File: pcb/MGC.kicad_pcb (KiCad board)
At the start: 2 copper layers, 92.7 x 62.2 mm, 121 parts, among them J1 USB_C_Receptacle, J10 Conn_01x04_Pin, J11 103R012BB100, J12 103R012BB100, J13 103R012BB100, J14 Conn_02x10_Odd_Even, J15 Conn_02x10_Odd_Even, J16 Conn_01x03, J17 Conn_01x01_Pin, J18 Conn_01x02_Pin, J19 Conn_01x02_Pin, J2 Conn_01x02_Pin, J20 Conn_01x02_Pin, J3 103R012BB100, J4 Conn_02x03_Odd_Even, J5 Conn_02x05_Odd_Even, J6 Conn_01x04, J7 103R012BB100, J8 Conn_01x01_Pin, J9 Conn_01x01_Pin, Q10 AO3416, Q11 AO3416, Q12 AO3416, Q13 AO3416, Q9 AO3416, SW0 SW_SPST, SW1 SW_SPST, SW2 SW_SPST, SW3 SW_SPST, SW5 SW_SPST, SW6 SW_DIP_x02, U1 FT230XS, U2 TS3USB30EDGSR, U3 74AHC1G14, U4 TPS2116DRL, U5 LM1117DT-3.3, U6 TBD62783A, U7 MB85RC04V

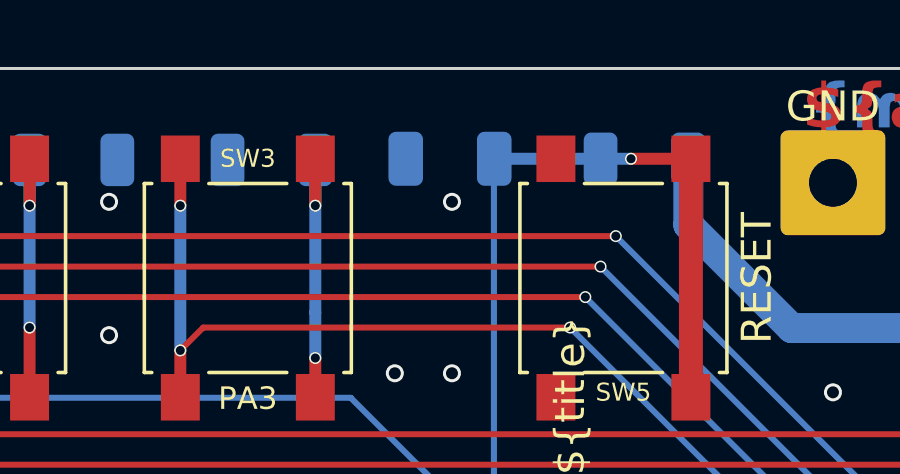
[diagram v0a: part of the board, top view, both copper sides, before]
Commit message: Change reset capacitor device size
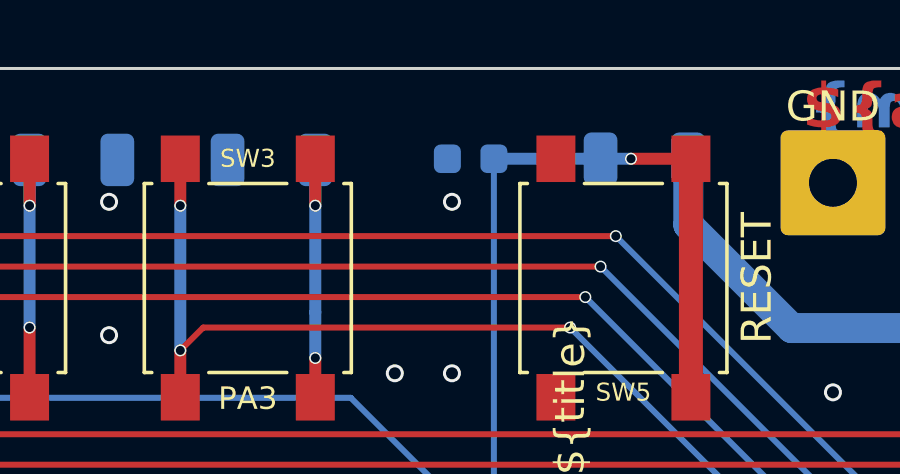
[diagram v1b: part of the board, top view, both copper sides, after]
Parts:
- C2: footprint Capacitor_SMD:C_1206_3216Metric -> Capacitor_SMD:C_0603_1608Metric
- moved C2 0.69 mm to (161.3, 66.5)
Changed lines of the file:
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@@
 		)
 	)
-	(footprint "Capacitor_SMD:C_1206_3216Metric"
+	(footprint "Capacitor_SMD:C_0603_1608Metric"
 		(layer "B.Cu")
-		(at 160.5895 66.51 180)
-		(descr "Capacitor SMD 1206 (3216 Metric), square (rectangular) end terminal, IPC-7351 nominal, (Body size source: IPC-SM-782 page 76, https://www.pcb-3d.com/wordpress/wp-content/uploads/ipc-sm-782a_amendment_1_and_2.pdf), generated with kicad-footprint-generator")
+		(at 161.277 66.51 180)
+		(descr "Capacitor SMD 0603 (1608 Metric), square (rectangular) end terminal, IPC-7351 nominal, (Body size source: IPC-SM-782 page 76, https://www.pcb-3d.com/wordpress/wp-content/uploads/ipc-sm-782a_amendment_1_and_2.pdf), generated with kicad-footprint-generator")
 		(tags "capacitor")
 		(property "Reference" "C2"
-			(at 0 1.506 0)
+			(at 0 1.1304 0)
 			(layer "B.SilkS")
 			(effects
@@
 					(size 0.6 0.6)
 					(thickness 0.12)
+					(bold yes)
 				)
 				(justify mirror)
@@
 		)
 		(property "Value" "10n"
-			(at 0 -1.85 0)
+			(at 0 -1.43 0)
 			(layer "B.Fab")
 			(effects
@@
 		(attr smd)
 		(fp_line
-			(start -0.711252 0.91)
-			(end 0.711252 0.91)
+			(start -0.14058 0.51)
+			(end 0.14058 0.51)
 			(stroke
 				(width 0.12)
@@
 		)
 		(fp_line
-			(start -0.711252 -0.91)
-			(end 0.711252 -0.91)
+			(start -0.14058 -0.51)
+			(end 0.14058 -0.51)
 			(stroke
 				(width 0.12)
@@
 		)
 		(fp_rect
-			(start -2.3 1.15)
-			(end 2.3 -1.15)
+			(start -1.48 0.73)
+			(end 1.48 -0.73)
 			(stroke
 				(width 0.05)
@@
 		)
 		(fp_rect
-			(start -1.6 0.8)
-			(end 1.6 -0.8)
+			(start -0.8 0.4)
+			(end 0.8 -0.4)
 			(stroke
 				(width 0.1)
@@
 			(effects
 				(font
-					(size 0.8 0.8)
-					(thickness 0.12)
+					(size 0.4 0.4)
+					(thickness 0.06)
 				)
 				(justify mirror)
@@
 		)
 		(pad "1" smd roundrect
-			(at -1.475 0 180)
-			(size 1.15 1.8)
+			(at -0.775 0 180)
+			(size 0.9 0.95)
 			(layers "B.Cu" "B.Mask" "B.Paste")
-			(roundrect_rratio 0.217391)
+			(roundrect_rratio 0.25)
 			(net 8 "RESET")
 			(pintype "passive")
 		)
 		(pad "2" smd roundrect
-			(at 1.475 0 180)
-			(size 1.15 1.8)
+			(at 0.775 0 180)
+			(size 0.9 0.95)
 			(layers "B.Cu" "B.Mask" "B.Paste")
-			(roundrect_rratio 0.217391)
+			(roundrect_rratio 0.25)
 			(net 4 "GND")
 			(pintype "passive")
 		)
 		(embedded_fonts no)
-		(model "${KICAD9_3DMODEL_DIR}/Capacitor_SMD.3dshapes/C_1206_3216Metric.step"
+		(model "${KICAD9_3DMODEL_DIR}/Capacitor_SMD.3dshapes/C_0603_1608Metric.step"
 			(offset
 				(xyz 0 0 0)
@@
 	)
 	(segment
-		(start 162.052 90.424)
-		(end 162.052 66.51)
-		(width 0.2)
-		(layer "B.Cu")
-		(net 8)
-	)
-	(segment
 		(start 158.275 91.615)
 		(end 160.861 91.615)
@@
 	)
 	(segment
-		(start 160.861 91.615)
-		(end 162.052 90.424)
+		(start 162.052 90.424)
+		(end 162.052 66.51)
 		(width 0.2)
 		(layer "B.Cu")
@@
 		(layer "B.Cu")
 		(net 8)
+	)
+	(segment
+		(start 160.861 91.615)
+		(end 162.052 90.424)
+		(width 0.2)
+		(layer "B.Cu")
+		(net 8)

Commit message: Device repositioning
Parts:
- moved D15 1.42 mm to (151.4, 82.1), turned to -90 degrees
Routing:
- net VDD: track 349.2 -> 357.5 mm
- net GND: vias 119 -> 118
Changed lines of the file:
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@@
 	(footprint "Diode_SMD:D_MiniMELF"
 		(layer "B.Cu")
-		(at 152.174 80.961)
+		(at 151.384 82.136 -90)
 		(descr "Diode Mini-MELF (SOD-80, LL-34)")
 		(tags "LL34")
 		(property "Reference" "D15"
-			(at 0 2 0)
+			(at 0 2 90)
 			(layer "B.SilkS")
 			(effects
@@
 		)
 		(property "Value" "BAT43"
-			(at 0 -2 0)
+			(at 0 -2 90)
 			(layer "B.Fab")
 			(effects
@@
 		)
 		(property "Datasheet" "~"
-			(at 0 0 180)
+			(at 0 0 90)
 			(unlocked yes)
 			(layer "B.Fab")
@@
 		)
 		(property "Description" "Diode"
-			(at 0 0 180)
+			(at 0 0 90)
 			(unlocked yes)
 			(layer "B.Fab")
@@
 		)
 		(property "Sim.Device" "D"
-			(at 0 0 180)
+			(at 0 0 90)
 			(unlocked yes)
 			(layer "B.Fab")
@@
 		)
 		(property "Sim.Pins" "1=K 2=A"
-			(at 0 0 180)
+			(at 0 0 90)
 			(unlocked yes)
 			(layer "B.Fab")
@@
 		)
 		(property "HTL" "100206"
-			(at 0 0 0)
+			(at 0 0 270)
 			(unlocked yes)
 			(layer "B.Fab")
@@
 		(attr smd)
 		(fp_line
-			(start -2.66 -1.11)
-			(end 1.75 -1.11)
+			(start -2.66 1.11)
+			(end -2.66 -1.11)
 			(stroke
 				(width 0.12)
@@
 		)
 		(fp_line
-			(start -2.66 1.11)
-			(end -2.66 -1.11)
+			(start 1.75 1.11)
+			(end -2.66 1.11)
 			(stroke
 				(width 0.12)
@@
 		)
 		(fp_line
-			(start 1.75 1.11)
-			(end -2.66 1.11)
+			(start -2.66 -1.11)
+			(end 1.75 -1.11)
 			(stroke
 				(width 0.12)
@@
 		)
 		(fp_line
-			(start -2.65 -1.1)
-			(end -2.65 1.1)
+			(start -2.65 1.1)
+			(end 2.65 1.1)
 			(stroke
 				(width 0.05)
@@
 		)
 		(fp_line
-			(start -2.65 1.1)
-			(end 2.65 1.1)
+			(start 2.65 1.1)
+			(end 2.65 -1.1)
 			(stroke
 				(width 0.05)
@@
 		)
 		(fp_line
-			(start 2.65 -1.1)
-			(end -2.65 -1.1)
+			(start -2.65 -1.1)
+			(end -2.65 1.1)
 			(stroke
 				(width 0.05)
@@
 		)
 		(fp_line
-			(start 2.65 1.1)
-			(end 2.65 -1.1)
+			(start 2.65 -1.1)
+			(end -2.65 -1.1)
 			(stroke
 				(width 0.05)
@@
 		)
 		(fp_line
-			(start -1.65 -0.8)
-			(end -1.65 0.8)
+			(start -1.65 0.8)
+			(end 1.65 0.8)
 			(stroke
 				(width 0.1)
@@
 		)
 		(fp_line
-			(start -1.65 0.8)
-			(end 1.65 0.8)
+			(start 1.65 0.8)
+			(end 1.65 -0.8)
 			(stroke
 				(width 0.1)
@@
 		)
 		(fp_line
-			(start -0.75 0)
-			(end -0.35 0)
+			(start 0.25 0.4)
+			(end 0.25 -0.4)
 			(stroke
 				(width 0.1)
@@
 		)
 		(fp_line
-			(start -0.35 0)
-			(end -0.35 -0.55)
+			(start -0.75 0)
+			(end -0.35 0)
 			(stroke
 				(width 0.1)
@@
 		)
 		(fp_line
-			(start 0.25 -0.4)
-			(end -0.35 0)
+			(start -0.35 0)
+			(end -0.35 -0.55)
 			(stroke
 				(width 0.1)
@@
 		)
 		(fp_line
-			(start 0.25 0.4)
-			(end 0.25 -0.4)
+			(start 0.25 -0.4)
+			(end -0.35 0)
 			(stroke
 				(width 0.1)
@@
 		)
 		(fp_line
-			(start 1.65 -0.8)
-			(end -1.65 -0.8)
+			(start -1.65 -0.8)
+			(end -1.65 0.8)
 			(stroke
 				(width 0.1)
@@
 		)
 		(fp_line
-			(start 1.65 0.8)
-			(end 1.65 -0.8)
+			(start 1.65 -0.8)
+			(end -1.65 -0.8)
 			(stroke
 				(width 0.1)
@@
 		)
 		(fp_text user "${REFERENCE}"
-			(at 0 2 0)
+			(at 0 2 90)
 			(layer "B.Fab")
 			(effects
@@
 		)
 		(pad "1" smd roundrect
-			(at -1.75 0)
+			(at -1.75 0 270)
 			(size 1.3 1.7)
 			(layers "B.Cu" "B.Mask" "B.Paste")
@@
 		)
 		(pad "2" smd roundrect
-			(at 1.75 0)
+			(at 1.75 0 270)
 			(size 1.3 1.7)
 			(layers "B.Cu" "B.Mask" "B.Paste")
@@
 	)
 	(segment
-		(start 153.924 80.961)
+		(start 151.384 83.886)
 		(end 153.924 83.886)
 		(width 0.4)
@@
 	)
 	(via
-		(at 142.24 83.82)
-		(size 0.6)
-		(drill 0.4)
-		(layers "F.Cu" "B.Cu")
-		(free yes)
-		(net 4)
-	)
-	(via
 		(at 192.786 80.264)
 		(size 0.4)
@@
 	)
 	(segment
-		(start 186.1 96.004)
-		(end 187.952 96.004)
+		(start 161.29 89.662)
+		(end 161.29 95.25)
 		(width 1)
 		(layer "F.Cu")
@@
 	)
 	(segment
-		(start 143.347 117.003)
-		(end 154.272 117.003)
+		(start 186.1 96.004)
+		(end 187.952 96.004)
 		(width 1)
 		(layer "F.Cu")
@@
 	)
 	(segment
-		(start 160.528 88.9)
-		(end 161.29 89.662)
+		(start 143.347 117.003)
+		(end 154.272 117.003)
 		(width 1)
 		(layer "F.Cu")
@@
 	)
 	(segment
-		(start 150.424 88.194)
-		(end 151.13 88.9)
-		(width 1)
-		(layer "F.Cu")
-		(net 7)
-	)
-	(segment
 		(start 185.1498 81.9)
 		(end 185.1498 81.224)
@@
 	)
 	(segment
-		(start 154.272 117.003)
-		(end 155.702 115.573)
+		(start 160.528 88.9)
+		(end 161.29 89.662)
 		(width 1)
 		(layer "F.Cu")
@@
 	)
 	(segment
-		(start 155.702 101.6)
-		(end 157.226 100.076)
+		(start 154.272 117.003)
+		(end 155.702 115.573)
 		(width 1)
 		(layer "F.Cu")
@@
 	)
 	(segment
-		(start 161.29 89.662)
-		(end 161.29 95.25)
+		(start 155.702 101.6)
+		(end 157.226 100.076)
 		(width 1)
 		(layer "F.Cu")
@@
 	)
 	(segment
-		(start 187.952 96.004)
-		(end 187.96 96.012)
+		(start 146.812 88.9)
+		(end 160.528 88.9)
 		(width 1)
 		(layer "F.Cu")
@@
 	)
 	(segment
-		(start 161.29 96.012)
-		(end 161.29 95.25)
+		(start 137.668 79.756)
+		(end 146.812 88.9)
 		(width 1)
 		(layer "F.Cu")
@@
 	)
 	(segment
-		(start 151.384 100.076)
-		(end 150.495 100.965)
+		(start 187.952 96.004)
+		(end 187.96 96.012)
 		(width 1)
 		(layer "F.Cu")
@@
 	)
 	(segment
-		(start 185.155 87.111)
-		(end 185.155 83.193207)
+		(start 161.29 96.012)
+		(end 161.29 95.25)
 		(width 1)
 		(layer "F.Cu")
@@
 	)
 	(segment
-		(start 150.424 83.185)
-		(end 150.424 88.194)
+		(start 151.384 100.076)
+		(end 150.495 100.965)
 		(width 1)
 		(layer "F.Cu")
@@
 	)
 	(segment
-		(start 186.1 96.004)
-		(end 162.044 96.004)
+		(start 185.155 87.111)
+		(end 185.155 83.193207)
 		(width 1)
 		(layer "F.Cu")
@@
 	)
 	(segment
-		(start 151.13 88.9)
-		(end 160.528 88.9)
+		(start 186.1 96.004)
+		(end 162.044 96.004)
 		(width 1)
 		(layer "F.Cu")
@@
 	)
 	(via
-		(at 150.424 83.185)
-		(size 1)
-		(drill 0.6)
-		(layers "F.Cu" "B.Cu")
-		(net 7)
-	)
-	(via
-		(at 150.424 85.09)
+		(at 138.557 80.645)
 		(size 1)
 		(drill 0.6)
@@
 	)
 	(via
+		(at 137.668 79.756)
+		(size 1)
+		(drill 0.6)
+		(layers "F.Cu" "B.Cu")
+		(net 7)
+	)
+	(via
 		(at 185.166 87.122)
 		(size 1)
@@
 	)
 	(segment
-		(start 144.78 80.961)
-		(end 150.424 80.961)
-		(width 1)
-		(layer "B.Cu")
-		(net 7)
-	)
-	(segment
 		(start 185.166 87.122)
 		(end 185.166 95.242)
@@
 	)
 	(segment
+		(start 137.668 79.756)
+		(end 138.557 80.645)
+		(width 1)
+		(layer "B.Cu")
+		(net 7)
+	)
+	(segment
 		(start 130.937 100.965)
 		(end 130.81 100.838)
@@
 	(segment
 		(start 136.398 78.486)
-		(end 138.873 80.961)
+		(end 137.668 79.756)
 		(width 1)
 		(layer "B.Cu")
@@
 	)
 	(segment
-		(start 150.424 80.961)
-		(end 150.424 83.185)
+		(start 150.809 80.961)
+		(end 151.384 80.386)
 		(width 1)
 		(layer "B.Cu")
@@
 	)
 	(segment
+		(start 138.557 80.645)
+		(end 138.873 80.961)
+		(width 1)
+		(layer "B.Cu")
+		(net 7)
+	)
+	(segment
 		(start 115.57 101.092)
 		(end 115.57 87.376)
@@
 	)
 	(segment
+		(start 144.78 80.961)
+		(end 150.809 80.961)
+		(width 1)
+		(layer "B.Cu")
+		(net 7)
+	)
+	(segment
 		(start 127 78.486)
 		(end 129.54 78.486)
@@
 		(width 1)
 		(layer "B.Cu")
-		(net 7)
-	)
-	(segment
-		(start 150.424 83.185)
-		(end 150.424 85.09)
-		(width 1)
-		(layer "B.Cu")

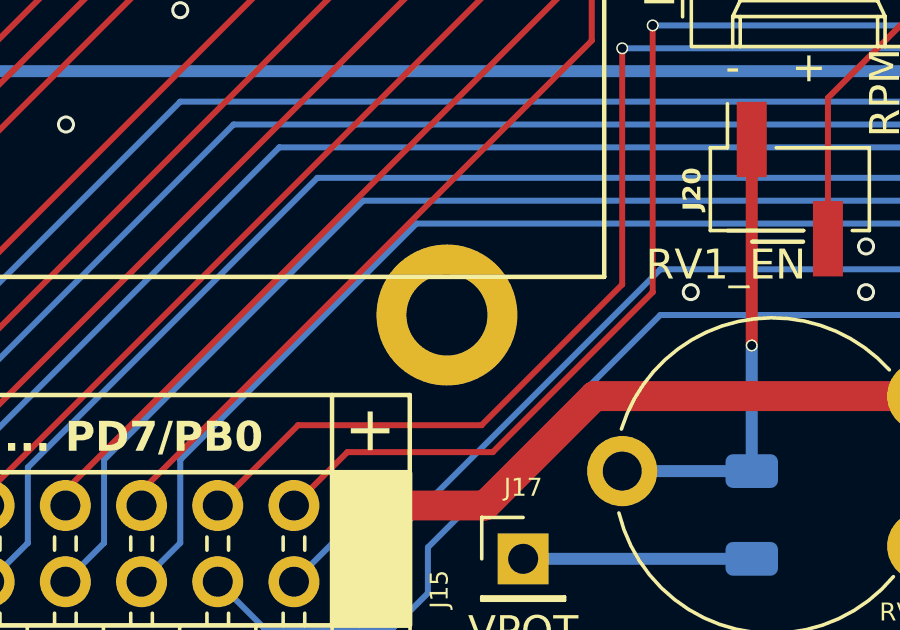
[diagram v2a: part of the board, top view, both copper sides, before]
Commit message: Move display mounting hole
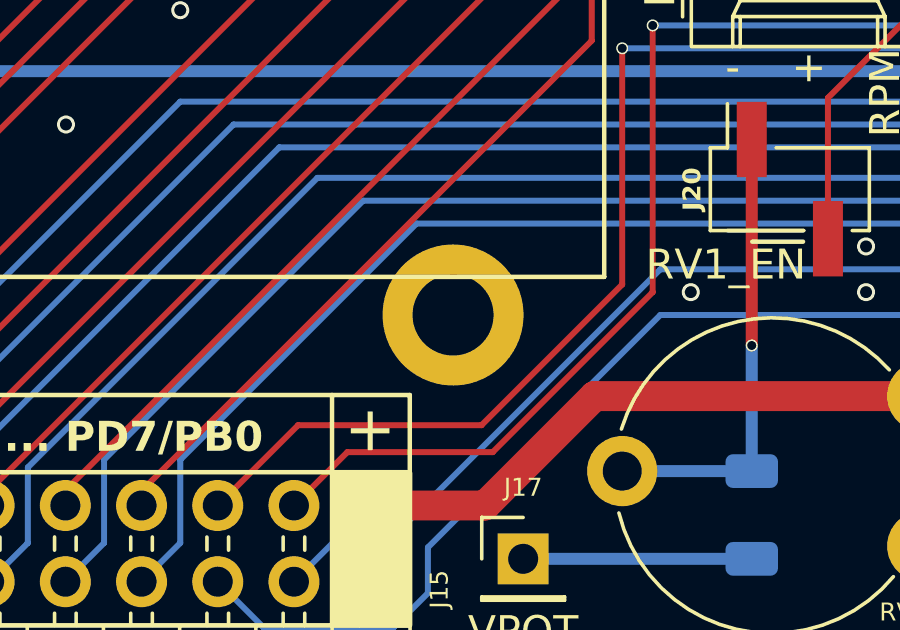
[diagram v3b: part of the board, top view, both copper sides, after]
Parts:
- moved H2 0.20 mm to (138.6, 114.3)
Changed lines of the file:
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@@
 	)
 	(footprint "MountingHole:MountingHole_2.7mm_M2.5_DIN965_Pad"
-		(locked yes)
 		(layer "F.Cu")
-		(at 138.43 114.3 90)
+		(at 138.6332 114.3 90)
 		(descr "Mounting Hole 2.7mm, M2.5, generated by kicad-footprint-generator mountinghole.py")
 		(tags "mountinghole M2.5 DIN965")
@@
 		(layer "Dwgs.User")
 		(pts
-			(xy 138.43 114.3) (xy 101.6 114.3)
+			(xy 165.989 84.963) (xy 174.879 84.963)
 		)
-		(height 24.13)
+		(height -22.733)
 		(orientation 0)
 		(format
@@
 			(keep_text_aligned yes)
 		)
-		(gr_text "36.83"
-			(at 120.015 137.28 0)
+		(gr_text "8.89"
+			(at 170.434 61.08 0)
 			(layer "Dwgs.User")
 			(effects
@@
 		(layer "Dwgs.User")
 		(pts
-			(xy 165.989 84.963) (xy 174.879 84.963)
+			(xy 101.6 63.5) (xy 194.31 63.5)
 		)
-		(height -22.733)
+		(height -3.81)
 		(orientation 0)
 		(format
@@
 			(keep_text_aligned yes)
 		)
-		(gr_text "8.89"
-			(at 170.434 61.08 0)
+		(gr_text "92.71"
+			(at 147.955 58.54 0)
 			(layer "Dwgs.User")
 			(effects
@@
 		(layer "Dwgs.User")
 		(pts
-			(xy 101.6 63.5) (xy 194.31 63.5)
+			(xy 105.41 67.31) (xy 101.6 67.31)
 		)
-		(height -3.81)
+		(height -5.08)
 		(orientation 0)
 		(format
@@
 			(keep_text_aligned yes)
 		)
-		(gr_text "92.71"
-			(at 147.955 58.54 0)
+		(gr_text "3.81"
+			(at 103.505 61.08 0)
 			(layer "Dwgs.User")
 			(effects
@@
 		(layer "Dwgs.User")
 		(pts
-			(xy 105.41 67.31) (xy 101.6 67.31)
+			(xy 116.84 114.3) (xy 116.84 63.5)
 		)
-		(height -5.08)
-		(orientation 0)
+		(height 82.55)
+		(orientation 1)
 		(format
 			(prefix "")
@@
 			(keep_text_aligned yes)
 		)
-		(gr_text "3.81"
-			(at 103.505 61.08 0)
+		(gr_text "50.8"
+			(at 198.24 88.9 90)
 			(layer "Dwgs.User")
 			(effects
@@
 		(layer "Dwgs.User")
 		(pts
-			(xy 116.84 114.3) (xy 116.84 63.5)
+			(xy 101.6 63.5) (xy 101.6 125.73)
 		)
-		(height 82.55)
+		(height -5.08)
 		(orientation 1)
 		(format
@@
 			(keep_text_aligned yes)
 		)
-		(gr_text "50.8"
-			(at 198.24 88.9 90)
+		(gr_text "62.23"
+			(at 95.37 94.615 90)
 			(layer "Dwgs.User")
 			(effects
@@
 		(layer "Dwgs.User")
 		(pts
-			(xy 101.6 63.5) (xy 101.6 125.73)
+			(xy 138.6332 114.3) (xy 101.6 114.3)
 		)
-		(height -5.08)
-		(orientation 1)
+		(height 24.13)
+		(orientation 0)
 		(format
 			(prefix "")
@@
 			(units 3)
 			(units_format 0)
-			(precision 4)
+			(precision 2)
 			(suppress_zeroes yes)
 		)
@@
 			(keep_text_aligned yes)
 		)
-		(gr_text "62.23"
-			(at 95.37 94.615 90)
+		(gr_text "37.03"
+			(at 120.1166 137.28 0)
 			(layer "Dwgs.User")
 			(effects
